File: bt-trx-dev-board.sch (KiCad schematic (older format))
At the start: 25 parts, among them J1 RJ45, J10 Conn_01x08, J2 PTT_BUTTON, J3 PTT_CON, J9 Conn_01x08, U1 SILabs_WT32i, U2 LTV-816S

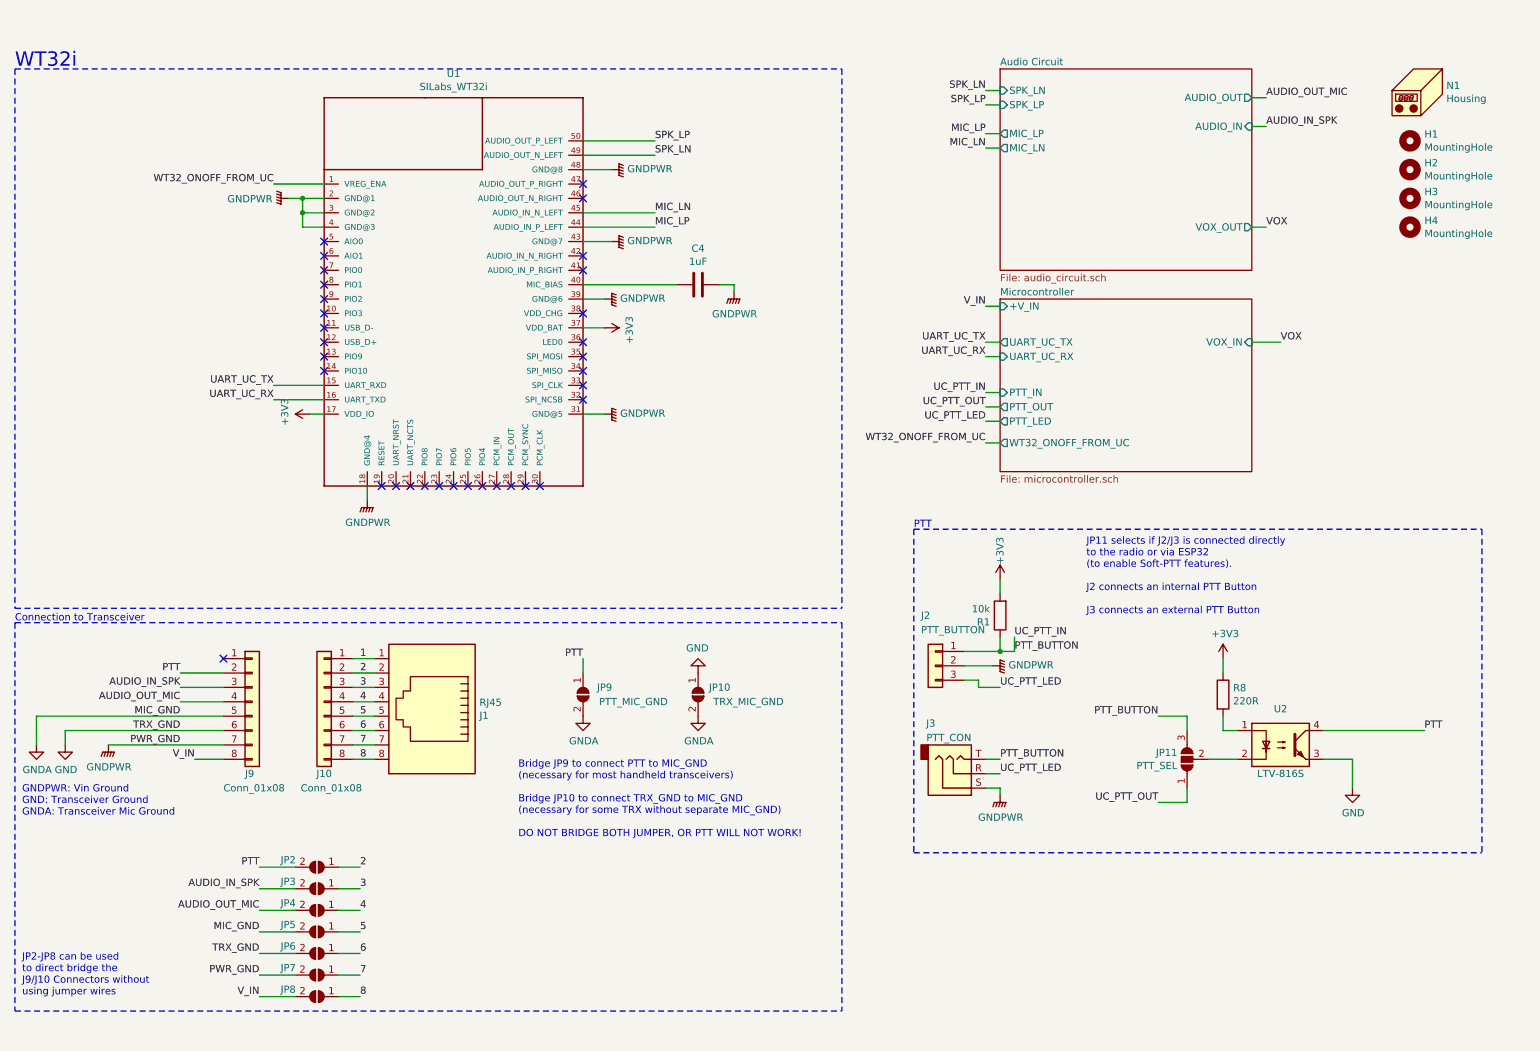
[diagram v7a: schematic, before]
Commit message: Continued V5.0 Schematic Rework [#21]
- Replaced PTT_SEL Jumper from solder to pinheader
- Added blockin capacitors to WT32i
- Removed J9/10 solder jumpers
- Added separate PTT GND
- Changed hardware version indicator to 3.3V
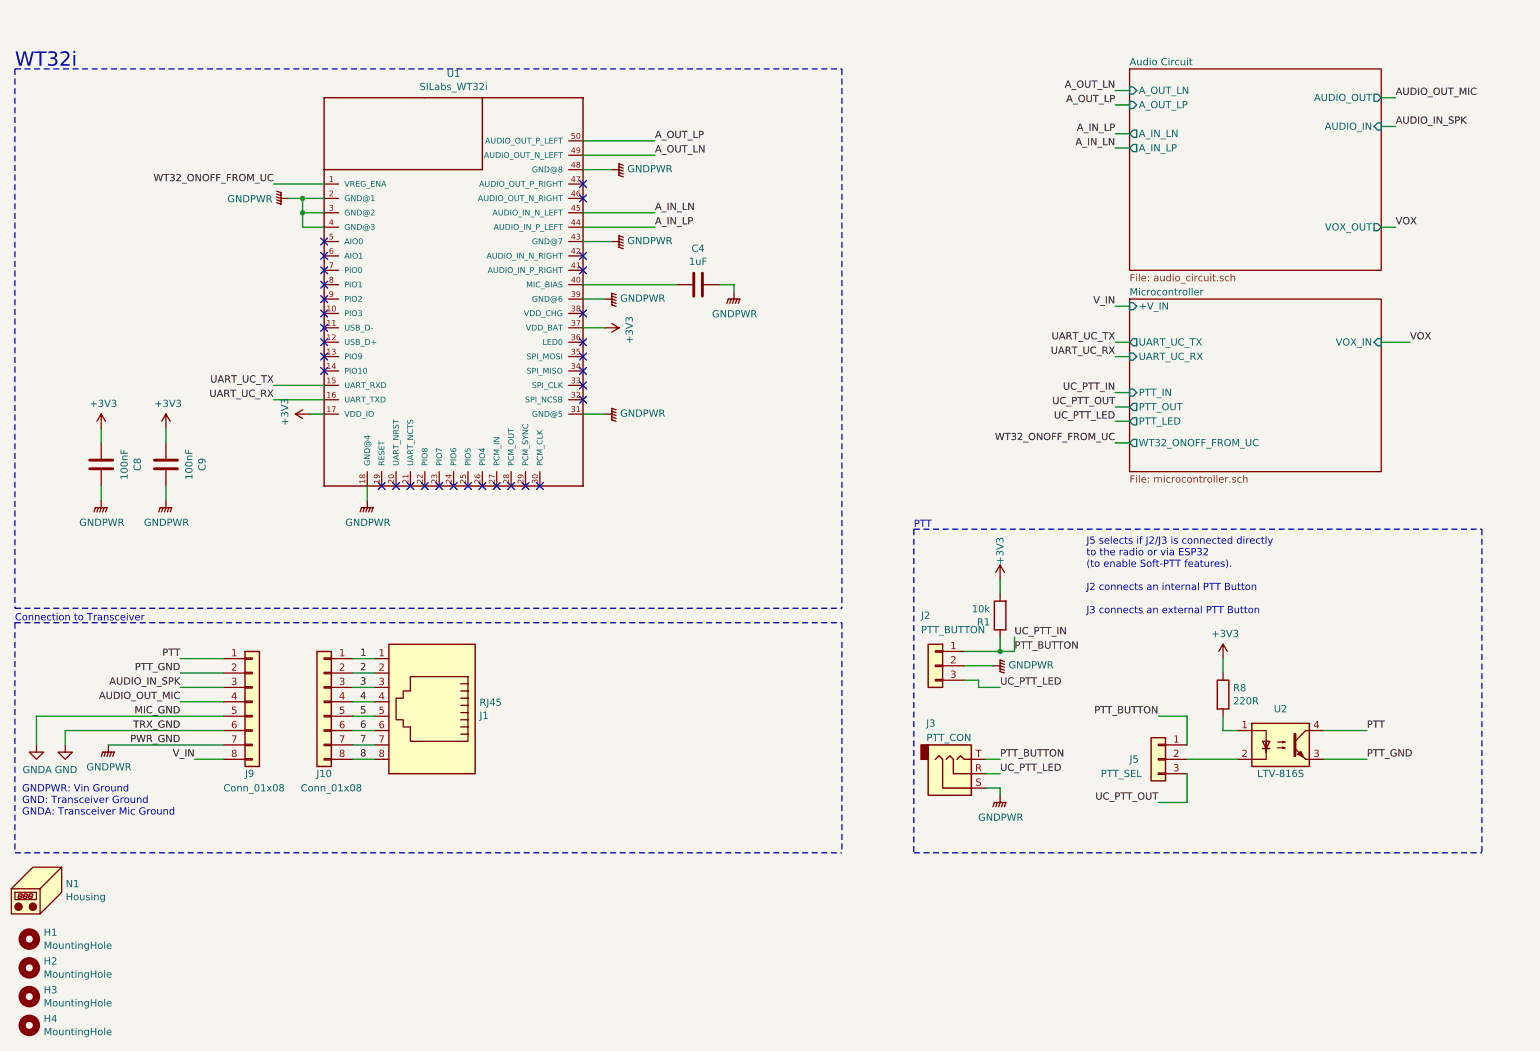
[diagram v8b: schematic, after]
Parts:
- removed JP10: TRX_MIC_GND, Jumper:SolderJumper-2_P1.3mm_Open_TrianglePad1.0x1.5mm, symbol Jumper:SolderJumper_2_Open
- removed JP11: PTT_SEL, Jumper:SolderJumper-3_P2.0mm_Open_TrianglePad1.0x1.5mm, symbol Jumper:SolderJumper_3_Open
- removed JP2: 2, Jumper:SolderJumper-2_P1.3mm_Open_TrianglePad1.0x1.5mm, symbol Jumper:SolderJumper_2_Open
- removed JP3: 3, Jumper:SolderJumper-2_P1.3mm_Open_TrianglePad1.0x1.5mm, symbol Jumper:SolderJumper_2_Open
- removed JP4: 4, Jumper:SolderJumper-2_P1.3mm_Open_TrianglePad1.0x1.5mm, symbol Jumper:SolderJumper_2_Open
- removed JP5: 5, Jumper:SolderJumper-2_P1.3mm_Open_TrianglePad1.0x1.5mm, symbol Jumper:SolderJumper_2_Open
- removed JP6: 6, Jumper:SolderJumper-2_P1.3mm_Open_TrianglePad1.0x1.5mm, symbol Jumper:SolderJumper_2_Open
- removed JP7: 7, Jumper:SolderJumper-2_P1.3mm_Open_TrianglePad1.0x1.5mm, symbol Jumper:SolderJumper_2_Open
- removed JP8: 8, Jumper:SolderJumper-2_P1.3mm_Open_TrianglePad1.0x1.5mm, symbol Jumper:SolderJumper_2_Open
- removed JP9: PTT_MIC_GND, Jumper:SolderJumper-2_P1.3mm_Open_TrianglePad1.0x1.5mm, symbol Jumper:SolderJumper_2_Open
- added C8, C9: 100nF, Capacitor_SMD:C_0805_2012Metric_Pad1.15x1.40mm_HandSolder, symbol Device:C
- added J5: PTT_SEL, Connector_PinHeader_2.54mm:PinHeader_1x03_P2.54mm_Vertical, symbol Connector_Generic:Conn_01x03
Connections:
- net +3V3: now also C8.2, C9.2
- net GND: no longer U2.3
- net GNDPWR: now also C8.1, C9.1
- net PTT: now also J9.1 (Pin_1); no longer J9.2 (Pin_2)
- net PTT_BUTTON: now also J5.1 (Pin_1)
- net UC_PTT_OUT: now also J5.3 (Pin_3)
- net at U2.2: now also J5.2 (Pin_2)
- net MIC_LN renamed A_IN_LN
- net MIC_LP renamed A_IN_LP
- net SPK_LN renamed A_OUT_LN
- net SPK_LP renamed A_OUT_LP
- new net PTT_GND: J9.2 (Pin_2), U2.3
- no-connect marks 33 -> 32
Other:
- note added: "J5 selects if J2/J3 is connected directly\nto the radio or via ESP32\n(to enable Soft-PTT features).\n\nJ2 connects an internal PTT Button\n\nJ3 connects an external PTT Button"
- note removed: "Bridge JP9 to connect PTT to MIC_GND \n(necessary for most handheld transceivers)\n\nBridge JP10 to connect TRX_GND to MIC_GND \n(necessary for some TRX without separate MIC_GND)\n\nDO NOT BRIDGE BOTH JUMPER, OR PTT WILL NOT WORK!"
- note removed: "JP11 selects if J2/J3 is connected directly\nto the radio or via ESP32\n(to enable Soft-PTT features).\n\nJ2 connects an internal PTT Button\n\nJ3 connects an external PTT Button"
- note removed: "JP2-JP8 can be used\nto direct bridge the\nJ9/J10 Connectors without\nusing jumper wires"
- moved on the sheet: H1, H2, H3, H4, N1
